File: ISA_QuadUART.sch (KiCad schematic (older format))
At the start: 77 parts, among them J1 ISA BUS, J10 Parallel Port, J11 Serial 4 IDC, J12 Serial 3 IDC, J13 UART4_SEL, J2 ADDR_IRQ, J3 UART1_SEL, J4 UART2_SEL, J5 ADDR, J6 Serial 2 IDC, J7 Serial 1 DB9, J8 UART3_SEL, J9 Parport IRQ Select, U1 74HCT138, U11 74LS30, U12 74LS86, U13 74LS02, U14 74LS155, U15 74LS245, U16 74LS174, U17 74LS374, U18 74LS05, U19 74LS125, U2 74HCT138, U20 74LS240, U21 74LS244, U23 16C554, U24 74HCT32, U25 GD75232N, U26 GD75232N, U29 74HCT245, U30 74HCT21, U5 GD75232N, U6 GD75232N, X1 1.8432Mhz

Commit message: Add first revision of single quad uart
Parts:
- removed C12, C13, C14, C15, C16, C36, C37, C38, C39, C40, C41: 100nF, Capacitor_THT:C_Disc_D6.0mm_W2.5mm_P5.00mm, symbol Device:C_Small
- removed C27, C28, C29, C30, C31, C32, C33, C34, C35: 2.2nF, Capacitor_THT:C_Disc_D5.0mm_W2.5mm_P5.00mm, symbol Device:C_Small
- removed J10: Parallel Port, Connector_PinHeader_2.54mm:PinHeader_2x13_P2.54mm_Vertical, symbol Connector_Generic:Conn_02x13_Odd_Even
- removed J9: Parport IRQ Select, Connector_PinHeader_2.54mm:PinHeader_2x04_P2.54mm_Vertical, symbol Connector_Generic:Conn_02x04_Odd_Even
- removed JP1: Address selection, Connector_PinHeader_2.54mm:PinHeader_1x02_P2.54mm_Vertical, symbol Device:Jumper_NO_Small
- removed JP2: Parport type, Connector_PinHeader_2.54mm:PinHeader_1x03_P2.54mm_Vertical, symbol Device:Jumper_NC_Dual
- removed RN1: 4.7k, Resistor_THT:R_Array_SIP9, symbol Device:R_Network08
- removed U11: 74LS30, Package_DIP:DIP-14_W7.62mm_LongPads, symbol 74xx:74LS30
- removed U12: 74LS86, Package_DIP:DIP-14_W7.62mm_LongPads, symbol 74xx:74LS86
- removed U13: 74LS02, Package_DIP:DIP-14_W7.62mm_LongPads, symbol 74xx:74LS02
- removed U14: 74LS155, Package_DIP:DIP-16_W7.62mm_LongPads, symbol 74xx:74LS155
- removed U15: 74LS245, Package_DIP:DIP-20_W7.62mm_LongPads, symbol 74xx:74LS245
- removed U16: 74LS174, Package_DIP:DIP-16_W7.62mm_LongPads, symbol 74xx:74LS174
- removed U17: 74LS374, Package_DIP:DIP-20_W7.62mm_LongPads, symbol 74xx:74LS374
- removed U18: 74LS05, Package_DIP:DIP-14_W7.62mm_LongPads, symbol 74xx:74LS05
- removed U19: 74LS125, Package_DIP:DIP-14_W7.62mm_LongPads, symbol 74xx:74LS125
- removed U20: 74LS240, Package_DIP:DIP-20_W7.62mm_LongPads, symbol 74xx:74LS240
- removed U21: 74LS244, Package_DIP:DIP-20_W7.62mm_LongPads, symbol 74xx:74LS244
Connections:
- no-connect marks 38 -> 34
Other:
- note removed: "Open - 0x278/9/A\nClosed - 0x378/9/A"
- note removed: "Parallel Port"
- moved on the sheet: C17, C18, C19, C20, C21, C22

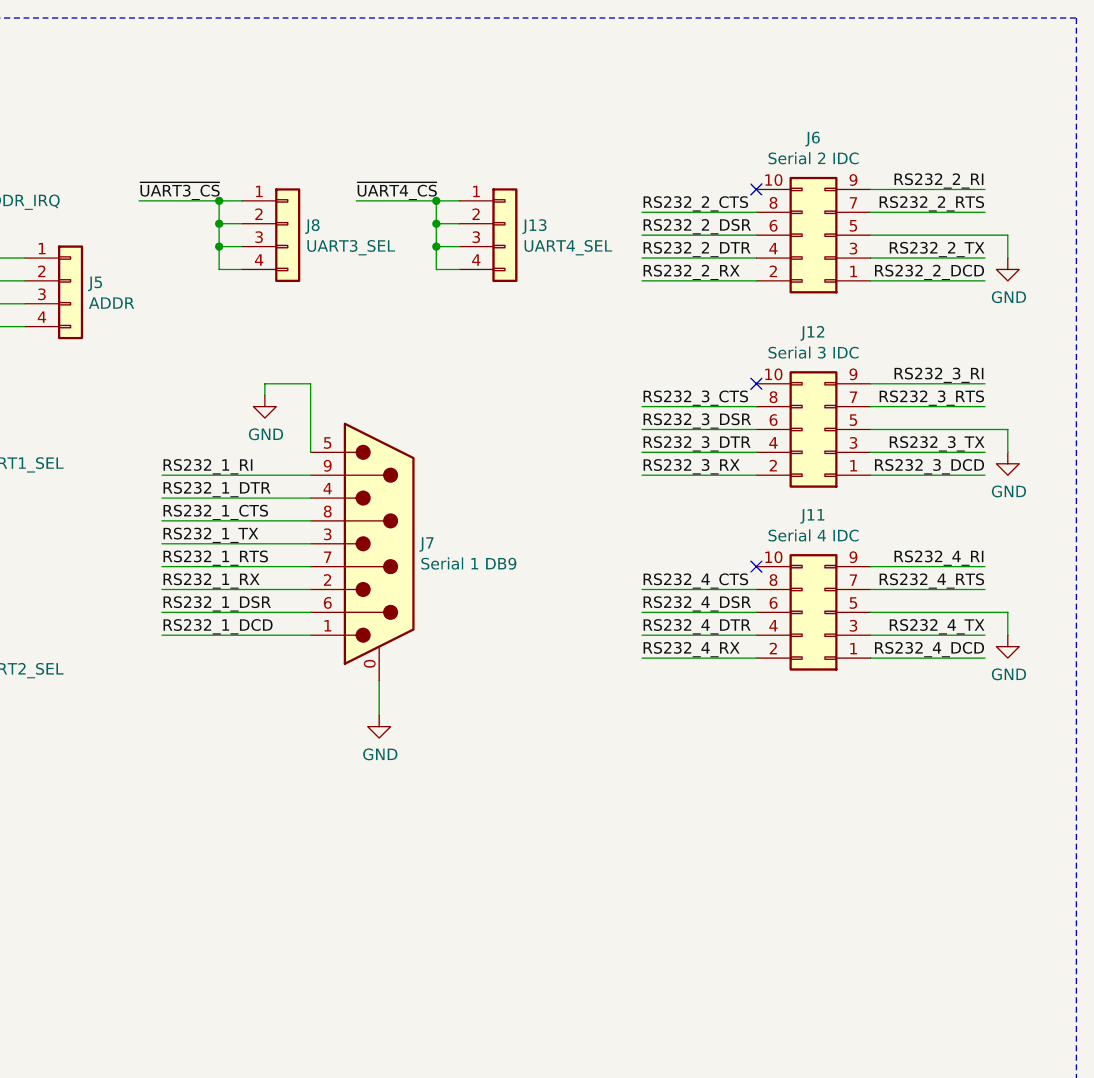
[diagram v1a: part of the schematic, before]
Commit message: Add 2 external serial ports
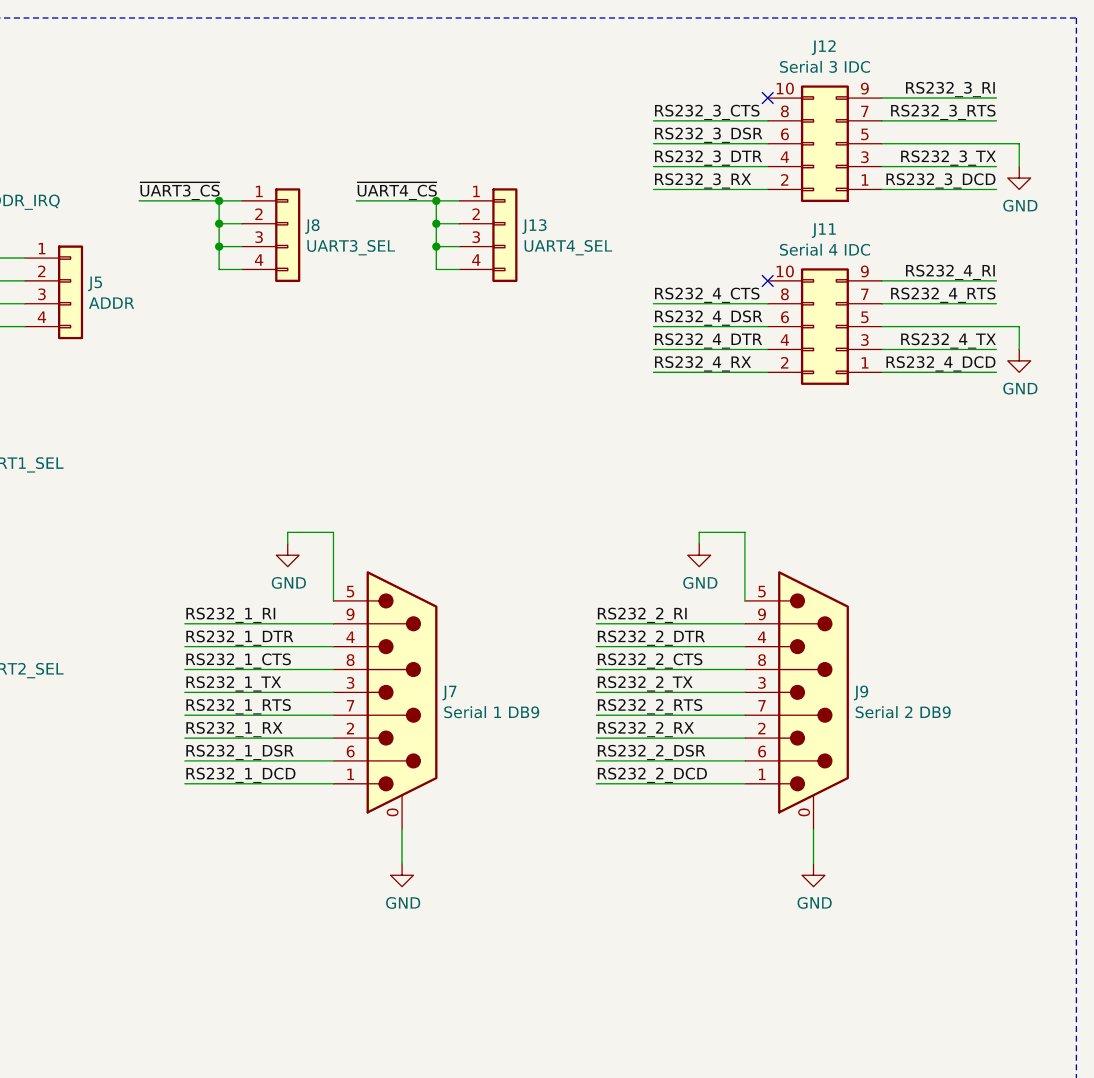
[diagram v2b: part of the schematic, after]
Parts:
- removed J6: Serial 2 IDC, Connector_PinHeader_2.54mm:PinHeader_2x05_P2.54mm_Vertical, symbol Connector_Generic:Conn_02x05_Odd_Even
- added J9: Serial 2 DB9, Connector_Dsub:DSUB-9_Male_Horizontal_P2.77x2.84mm_EdgePinOffset7.70mm_Housed_MountingHolesOffset9.12mm, symbol Connector:DB9_Male_MountingHoles
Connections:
- net GND: now also J9.0 (PAD), J9.5
- net RS232_2_CTS: now also J9.8
- net RS232_2_DCD: now also J9.1
- net RS232_2_DSR: now also J9.6
- net RS232_2_DTR: now also J9.4
- net RS232_2_RI: now also J9.9
- net RS232_2_RTS: now also J9.7
- net RS232_2_RX: now also J9.2
- net RS232_2_TX: now also J9.3
- no-connect marks 34 -> 33
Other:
- moved on the sheet: J11, J12, J7
